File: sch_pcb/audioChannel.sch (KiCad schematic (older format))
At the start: 90 parts, among them J201 TO_SOUNDCARD, J202 FROM_SOUNDCARD, J203 Radio Port, J404 DB9_FEMALE, Q201 2N7000, Q202 2N7000, Q203 2N7000, U103 MCP4351, U106 MCP4351, U201 MCP6004N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

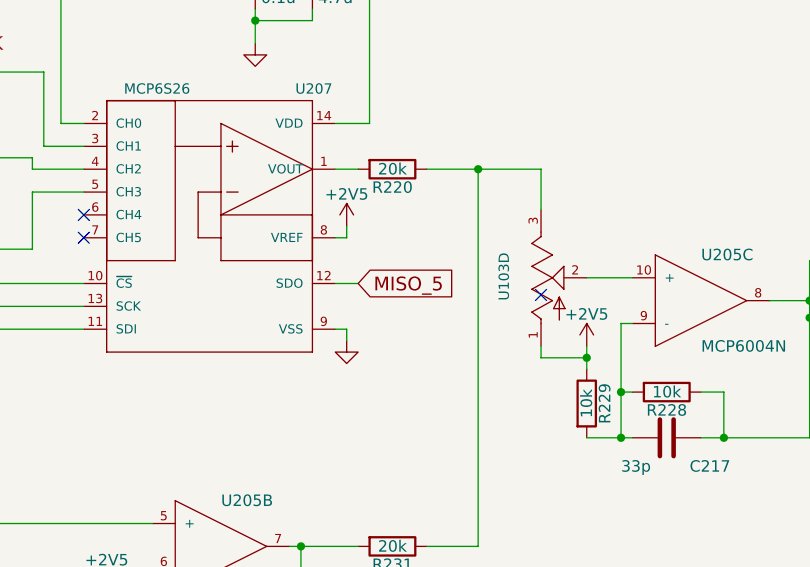
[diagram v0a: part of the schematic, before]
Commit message: Updates based on emails
Disconnect SDO on PGAs
Add mounting holes 
More placement on PCB - for now, delete all 4xx sheet footprints.  Once channel 1 is placed, it will get copied to make channel 2.
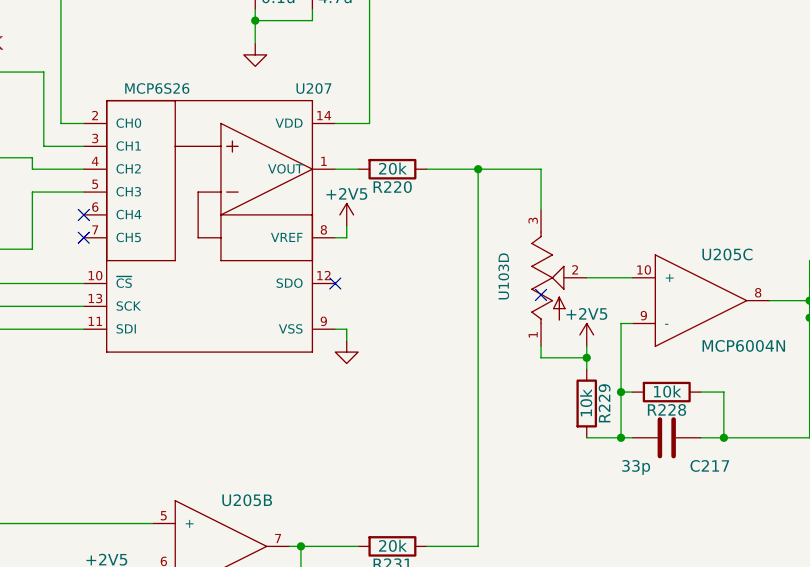
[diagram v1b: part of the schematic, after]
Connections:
- net MISO_5: no longer names the net of U207.12 (SDO)
- no-connect marks 11 -> 12
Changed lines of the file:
@@
 $Descr B 17000 11000
 encoding utf-8
-Sheet 2 4
+Sheet 4 4
 Title "PiPtr Audio"
 Date ""
@@
 Text GLabel 10525 5975 0    60   Input ~ 0
 MOSI_5
-Text GLabel 12300 5775 2    60   Input ~ 0
-MISO_5
-Wire Wire Line
-	12200 5775 12300 5775
 Wire Wire Line
 	10925 4850 10925 5175
@@
 	1    0    0    -1
 $EndComp
+NoConn ~ 12200 5775
 $EndSCHEMATC

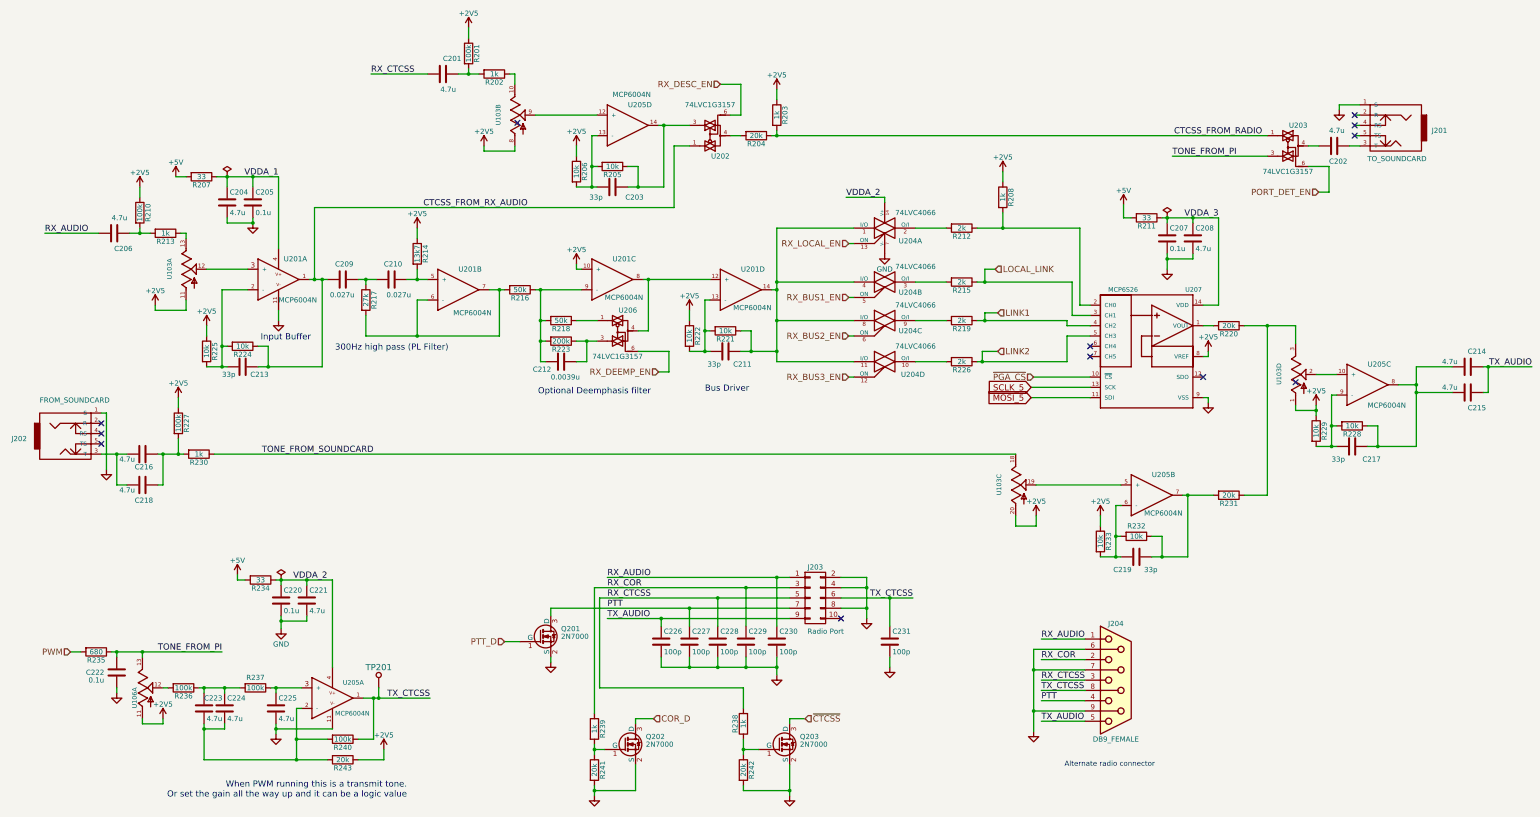
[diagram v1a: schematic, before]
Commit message: Add files via upload
Fix missing pin numbers on opamps
Change two 4.7uF caps in parallel to 10uF/0805.  This will save 6 caps and will handle capacitance loss due to DC bias better
Change 2 22uF caps to 4 10uF caps to get rid of an extra BOM line item
More work on placement.  The channel now fits in the space allocated to it. 
Connectors need to be revisited - GPIO and soundcard
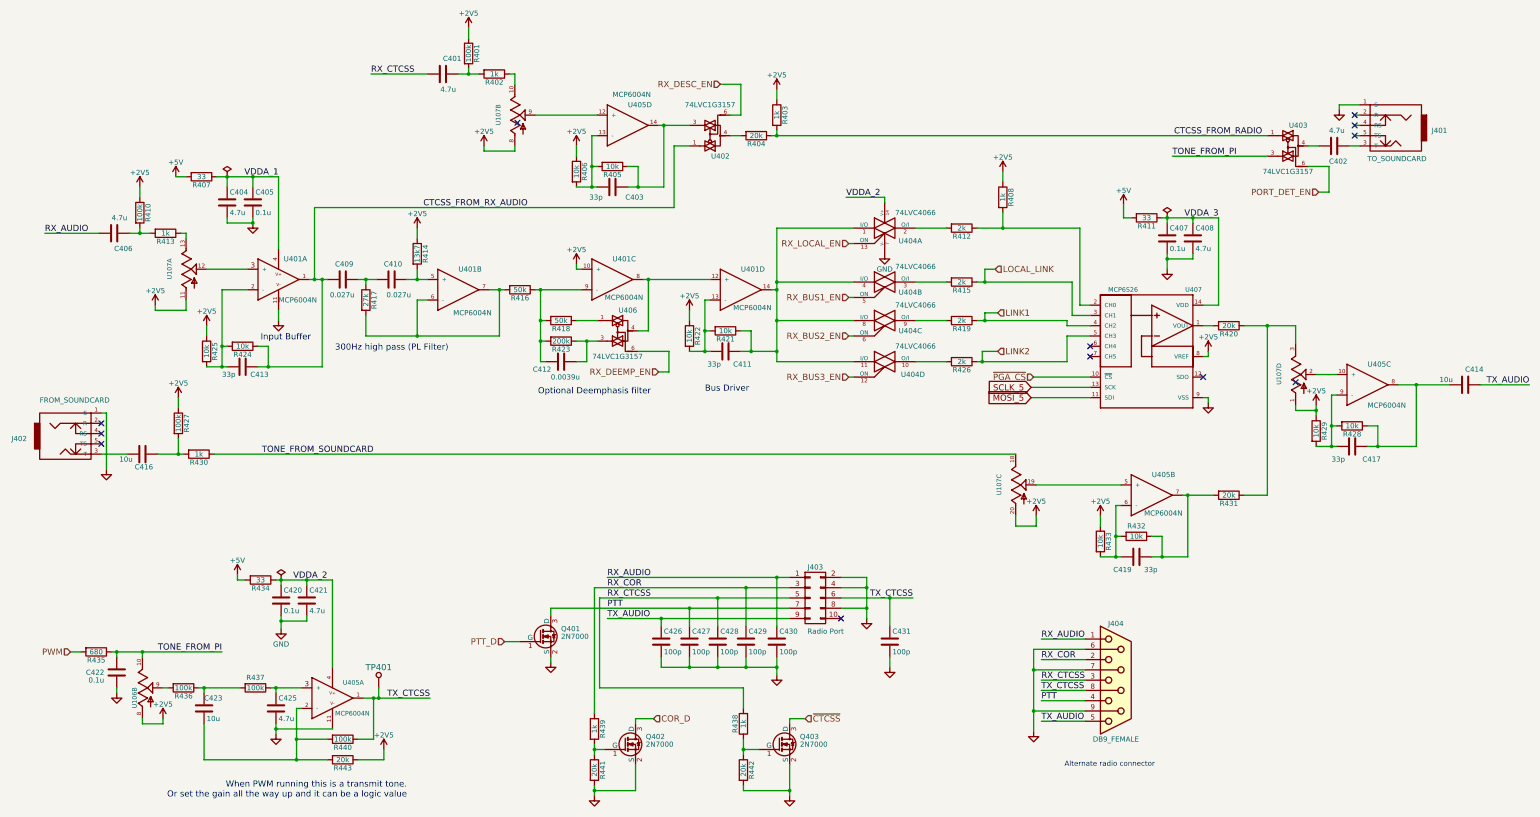
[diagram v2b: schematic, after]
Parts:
- removed C215, C218, C224: 4.7u, lib:smd0603, symbol C
- C214, C216, C223: value 4.7u -> 10u; footprint lib:smd0603 -> lib:smd0805
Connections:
- net +2V5: now also U106.8 (A); no longer U106.11 (A)
- net TONE_FROM_PI: now also U106.10 (B); no longer U106.13 (B)
- net at R236.2: now also U106.9 (W); no longer U106.12 (W)
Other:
- moved on the sheet: C414

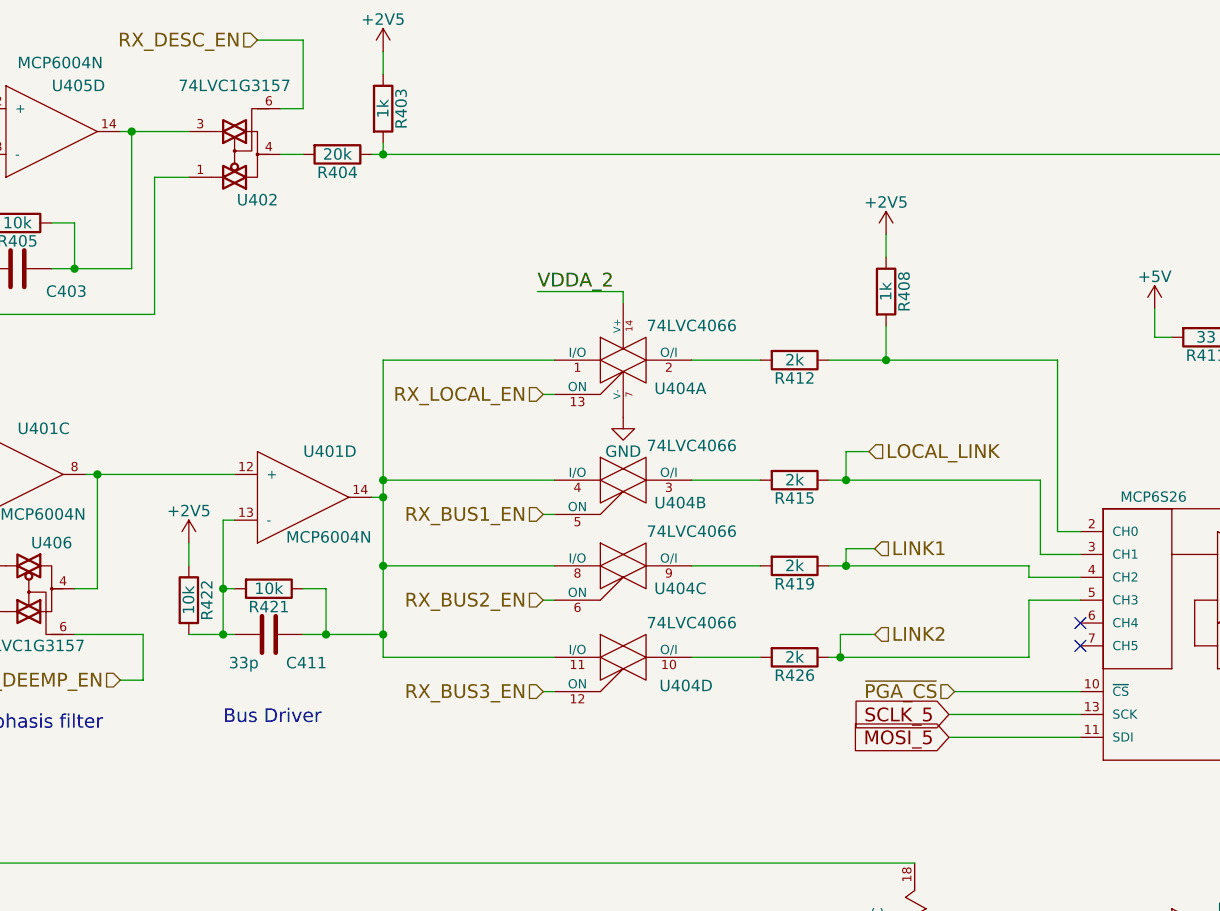
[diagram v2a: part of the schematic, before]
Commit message: Add files via upload
Changed  user_adc connector to 2x7 (14-pin is a lot more common than 12-pin)
Changed user_gpio connector to 2 2x8 connectors.  1x20 takes too much linear space
First pass layout on the two audio channels.  Right now, board is 4-layer, 100x150mm.  May be able to knock down the 150mm dimension 
The link and soundcard connectors fit in a row across the front edge.
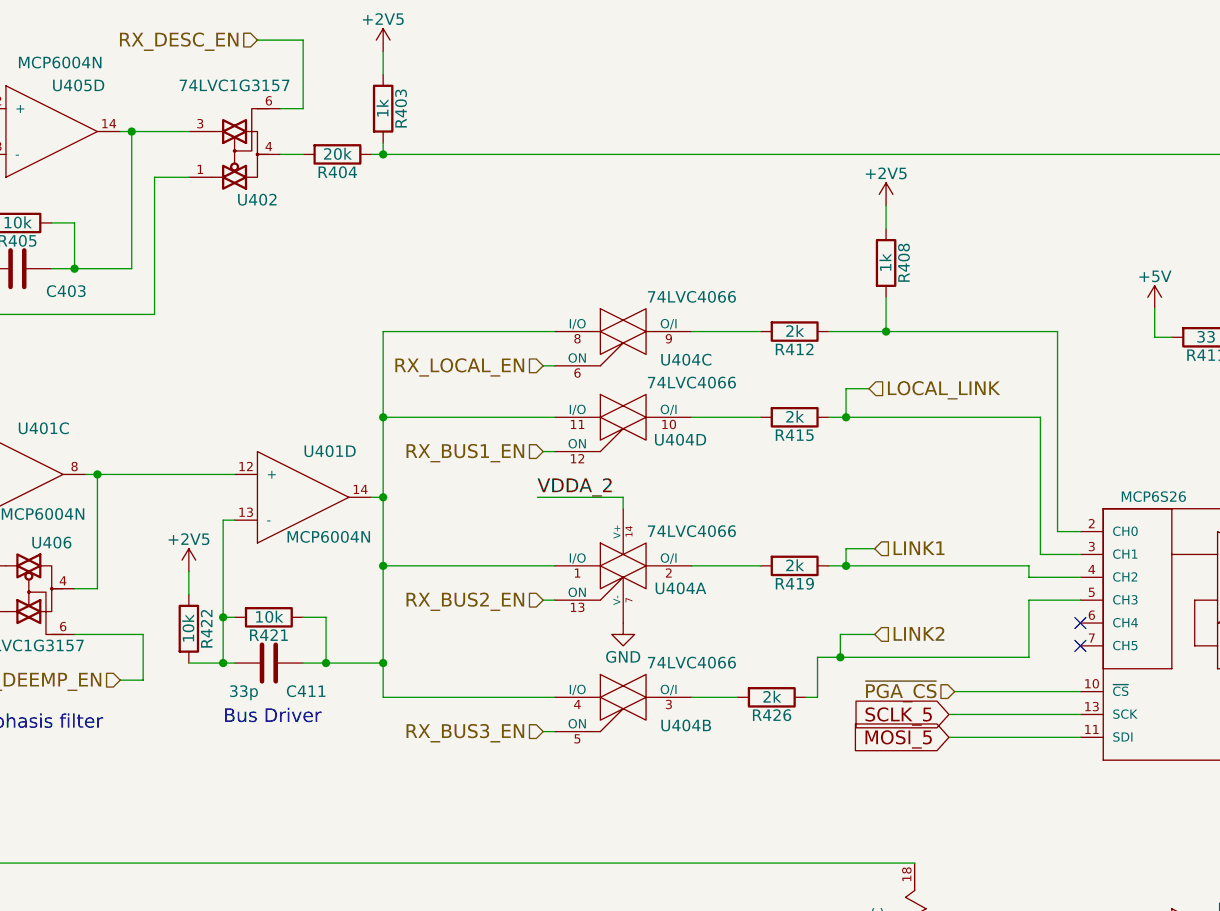
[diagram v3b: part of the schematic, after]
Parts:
- removed unit 1 of U204
- added unit 3 of U204
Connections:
- net GND: now also U204.7 (V-)
- net RX_BUS1_EN: now also U204.12 (ON); no longer U204.5 (ON)
- net RX_BUS2_EN: now also U204.13 (ON); no longer U204.6 (ON)
- net RX_BUS3_EN: now also U204.5 (ON); no longer U204.12 (ON)
- net RX_LOCAL_EN: now also U204.6 (ON)
- net VDDA_2: now also U204.14 (V+)
- net at C211.1, R221.1, U201.14 (OUT): now also U204.1 (I/O), U204.11 (I/O), U204.4 (I/O), U204.8 (I/O); no longer U204.11 (I/O), U204.4 (I/O), U204.8 (I/O)
- net at R212.2: now also U204.9 (O/I)
- net at R215.2: now also U204.10 (O/I); no longer U204.3 (O/I)
- net at R219.2: now also U204.2 (O/I); no longer U204.9 (O/I)
- net at R226.2: now also U204.3 (O/I); no longer U204.10 (O/I)
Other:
- moved on the sheet: C411, R408, R412, R415, R421, R422, R426

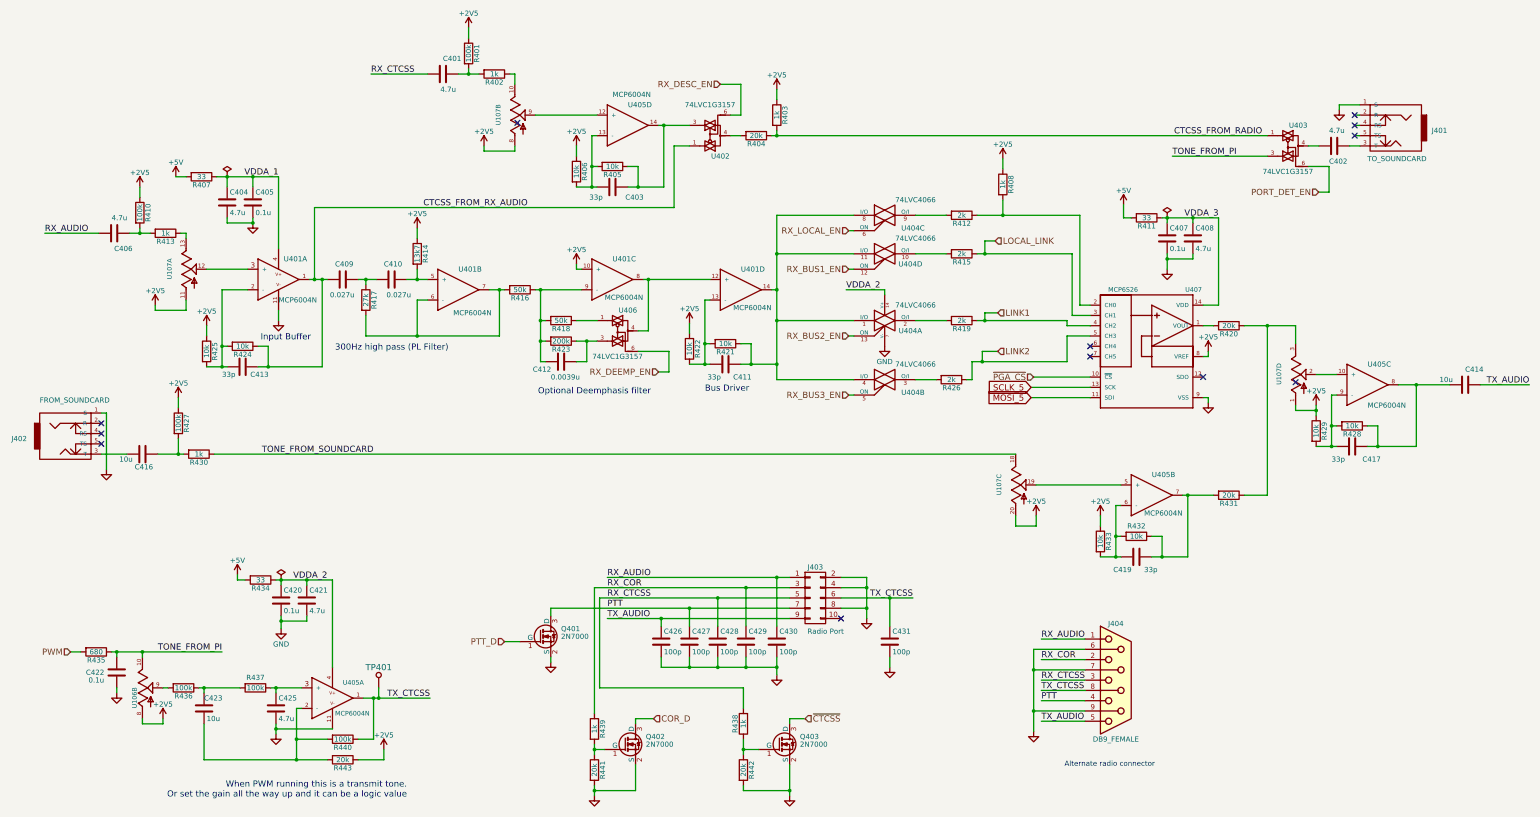
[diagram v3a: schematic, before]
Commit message: Add files via upload
Reversed ends on all pots so up increases level
Added outline and mounting holes to RasPi footprint so we can see how big it really is
Moved parts away from one of the RasPi mounting holes so we can use all 4 of them
More routing - finished user GPIO and ADC, SPI chipselect decoder
Still to do: level shifters, RasPi connections and spares
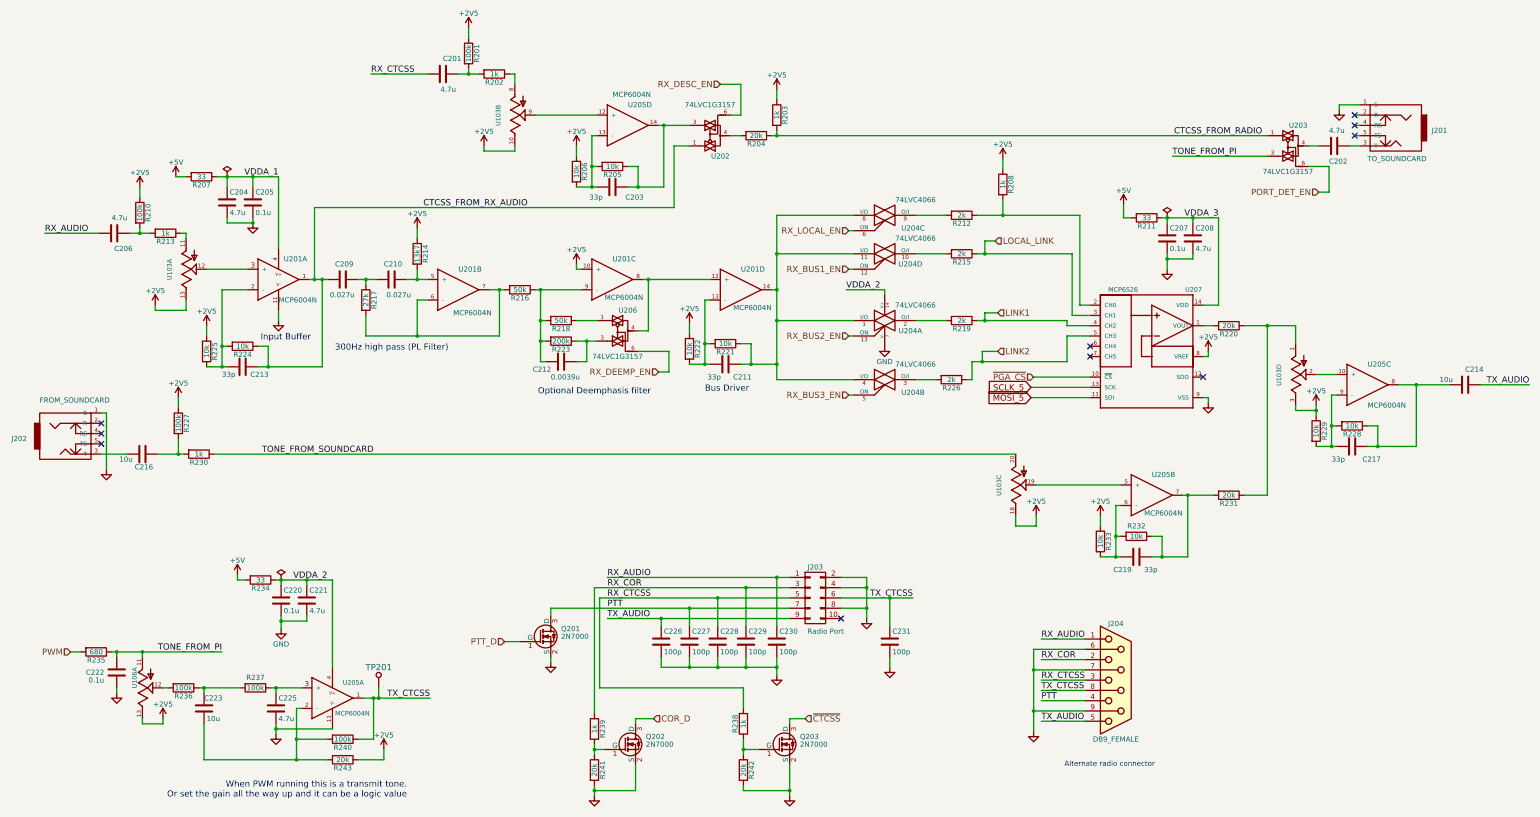
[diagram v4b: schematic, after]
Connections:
- net +2V5: now also U103.10 (B), U103.13 (B), U103.18 (B), U103.3 (B), U106.13 (B); no longer U103.1 (A), U103.11 (A), U103.20 (A), U103.8 (A), U106.8 (A)
- net TONE_FROM_PI: now also U106.11 (A); no longer U106.10 (B)
- net TONE_FROM_SOUNDCARD: now also U103.20 (A); no longer U103.18 (B)
- net at R213.1: now also U103.11 (A); no longer U103.13 (B)
- net at R202.1: now also U103.8 (A); no longer U103.10 (B)
- net at R220.1, R231.1: now also U103.1 (A); no longer U103.3 (B)
- net at R236.2: now also U106.12 (W); no longer U106.9 (W)
- no-connect marks 12 -> 10
